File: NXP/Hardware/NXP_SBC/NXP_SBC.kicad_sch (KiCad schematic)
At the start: 0 parts

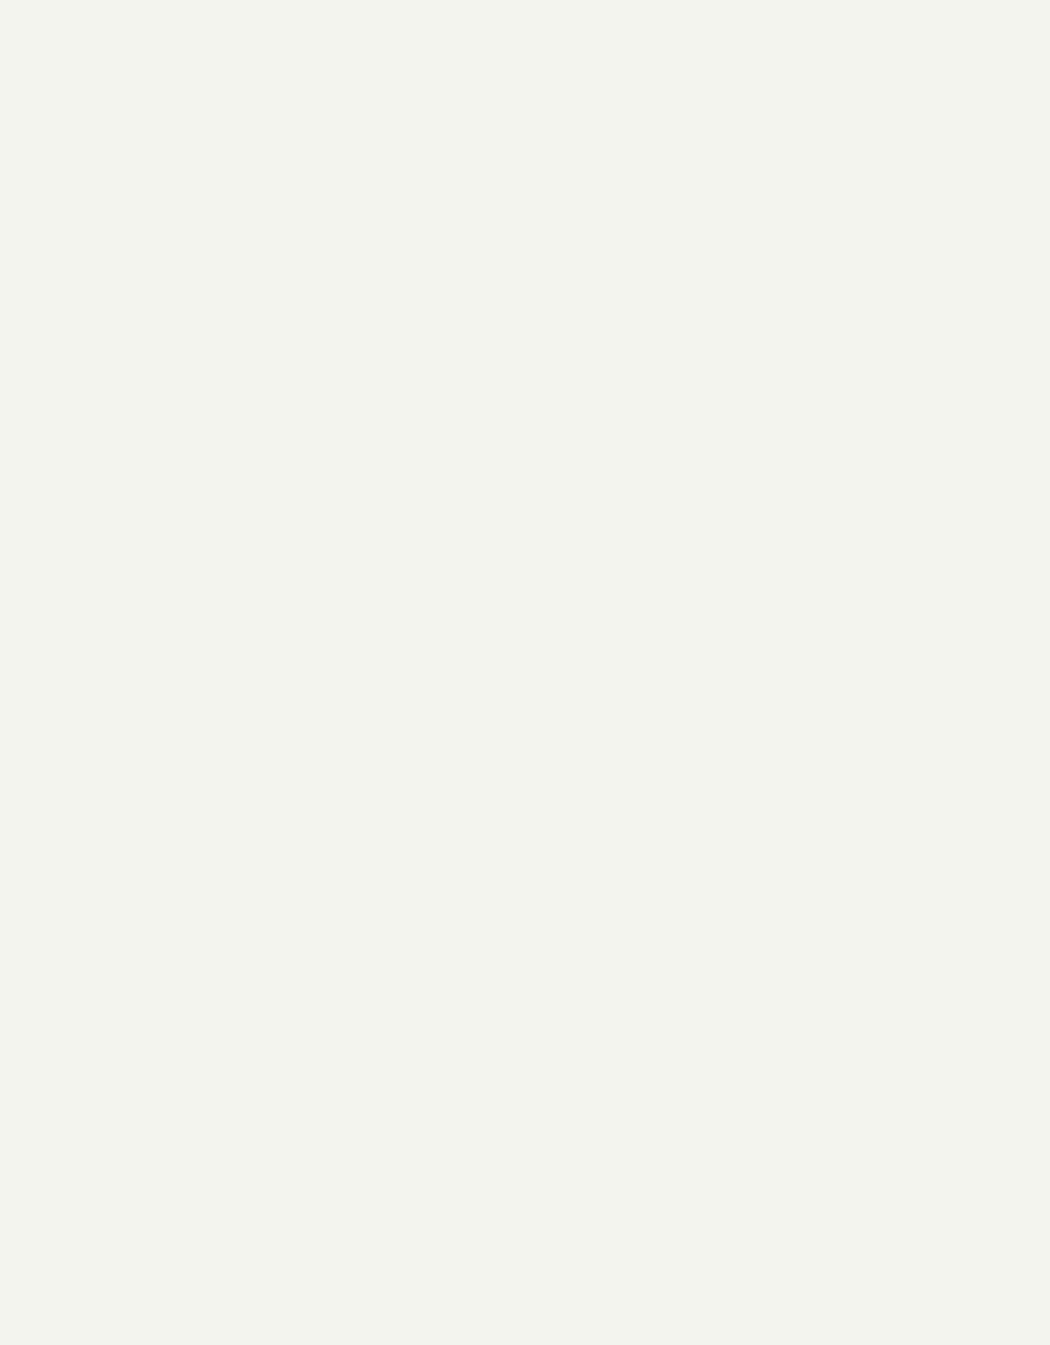
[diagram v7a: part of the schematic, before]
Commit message: added audio page
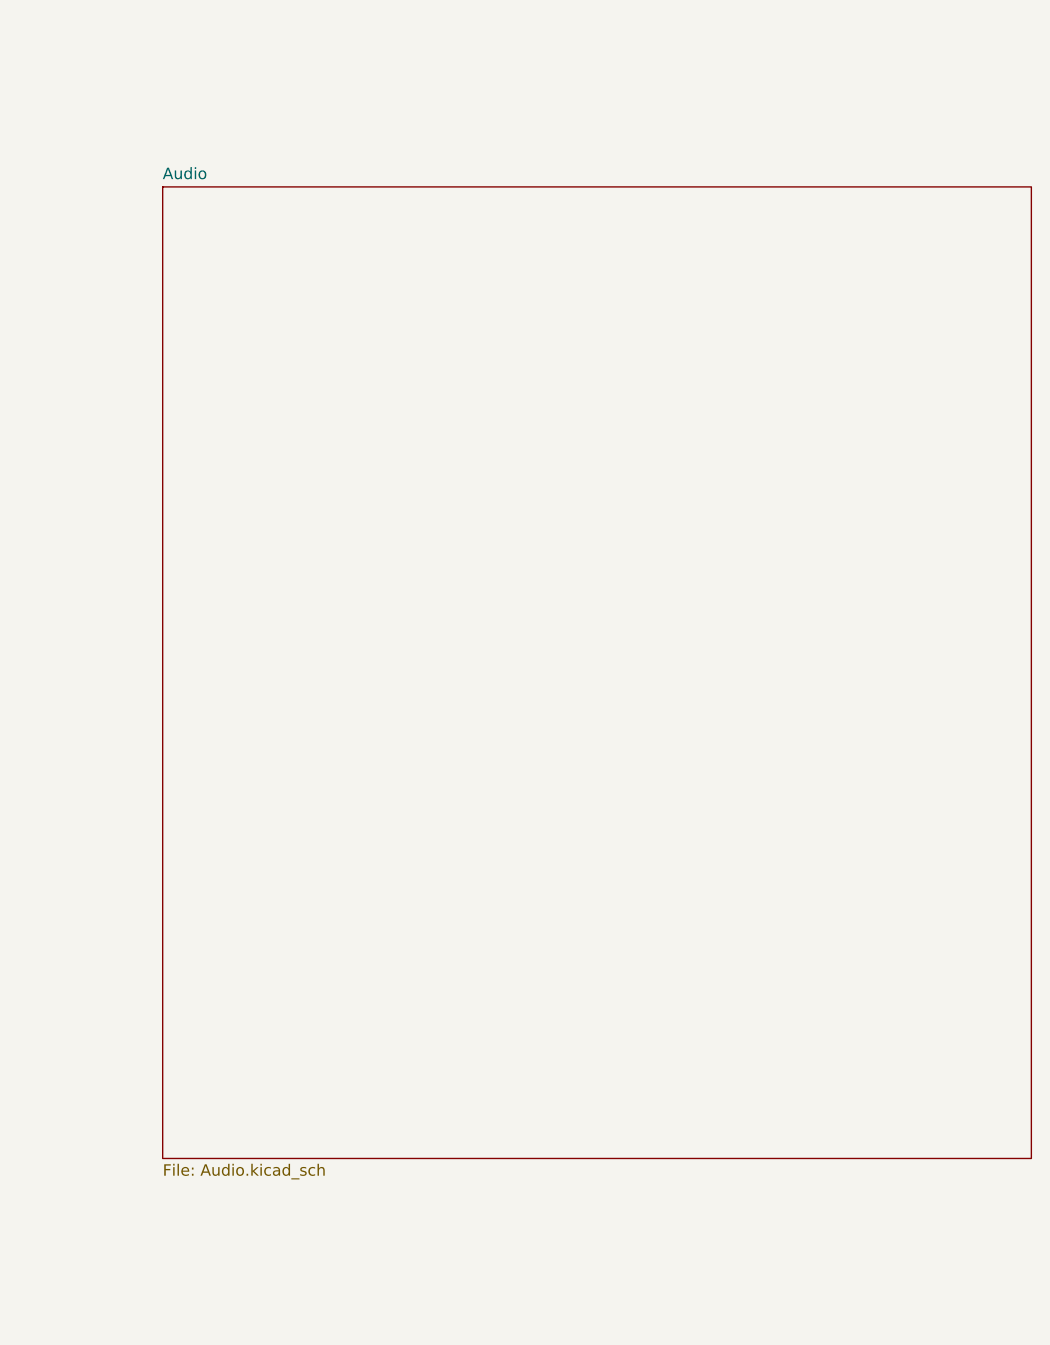
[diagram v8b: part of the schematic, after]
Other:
- added sheet Audio (Audio.kicad_sch)
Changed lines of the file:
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@@
+		)
+	)
+	(sheet
+		(at 530.86 322.58)
+		(size 96.52 107.95)
+		(exclude_from_sim no)
+		(in_bom yes)
+		(on_board yes)
+		(dnp no)
+		(fields_autoplaced yes)
+		(stroke
+			(width 0.1524)
+			(type solid)
+		)
+		(fill
+			(color 0 0 0 0.0000)
+		)
+		(property "Sheetname" "Audio"
+			(at 530.86 321.8684 0)
+			(effects
+				(font
+					(size 1.27 1.27)
+				)
+				(justify left bottom)
+			)
+		)
+		(property "Sheetfile" "Audio.kicad_sch"
+			(at 530.86 431.1146 0)
+			(effects
+				(font
+					(size 1.27 1.27)
+				)
+				(justify left top)
+			)
+		)
+		(instances
+			(project "NXP_SBC"
+				(path "/e82fc437-413b-4185-b609-66f66e24e498"
+					(page "8")
+				)
+			)
 		)
 	)
